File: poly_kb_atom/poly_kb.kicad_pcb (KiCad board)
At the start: 2 copper layers, 19.1 x 19 mm, 18 parts, among them J1 Conn_01x16, J2 North, J3 WestFront, J4 EastFront, J5 WestBack, J6 EastBack, J7 South, J8 North2, J9 South2, SW1 SW_Push

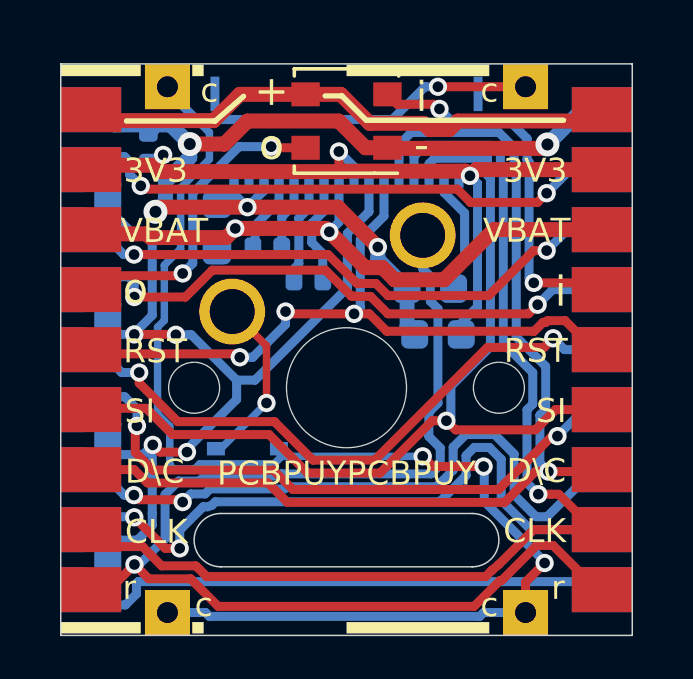
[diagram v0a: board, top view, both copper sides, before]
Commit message: Fixed wrong connection in between pin 16 an VCC in PolyAtom2; Added ConectorL
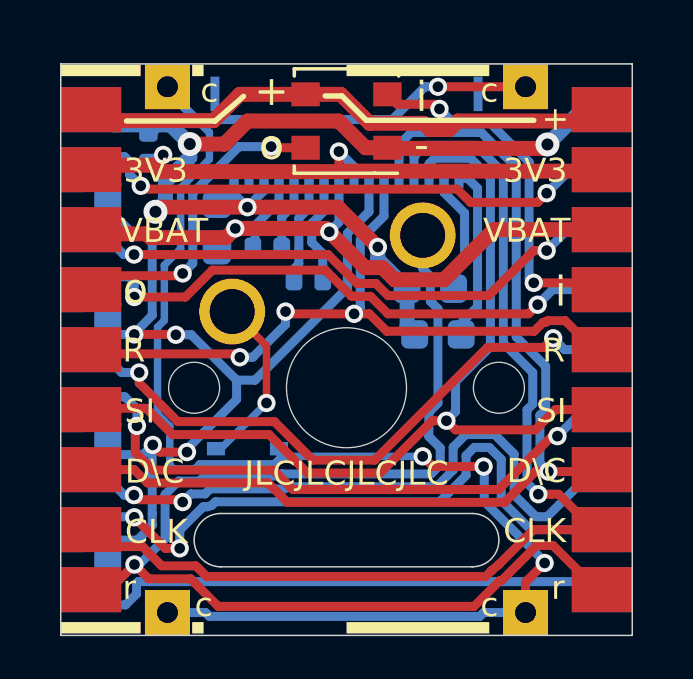
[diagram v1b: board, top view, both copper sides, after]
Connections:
- C1 pad 1: /Keyboard/sheet605ED2EB/3V3 -> Net-(C1-Pad1)
- J1 pad 16: /Keyboard/sheet605ED2EB/3V3 -> Net-(C1-Pad1)
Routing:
- net /Keyboard/sheet605ED2EB/3V3: track 25.8 -> 19.9 mm, vias 3 -> 2
- net Net-(C1-Pad1): track 0.00 -> 5.83 mm
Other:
- board text added: "+"
- board text added: ".1"
- board text added: "JLCJLCJLCJLC"
- board text added: "R"
- board text removed: "PCBPUYPCBPUY"
- board text removed: "RST"

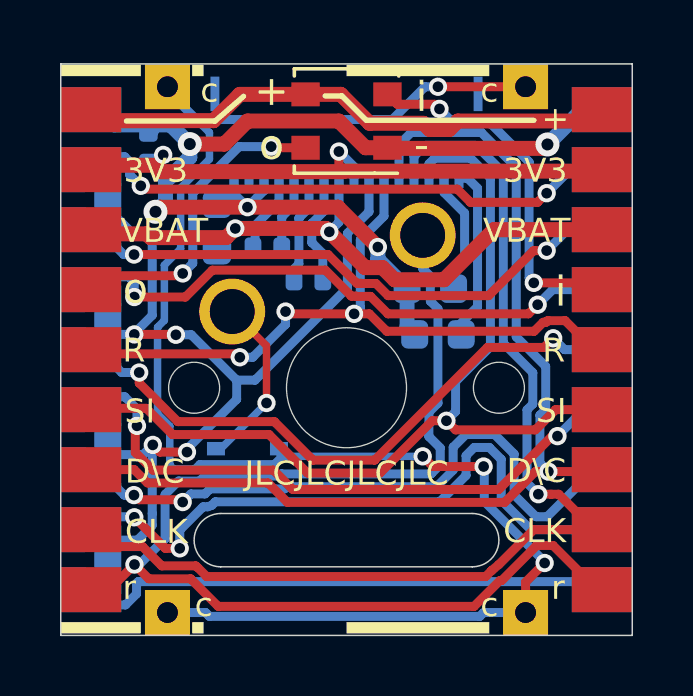
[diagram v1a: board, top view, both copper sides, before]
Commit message: Update to Kicad6 for PolyAtom and added a pullup resistor for CS
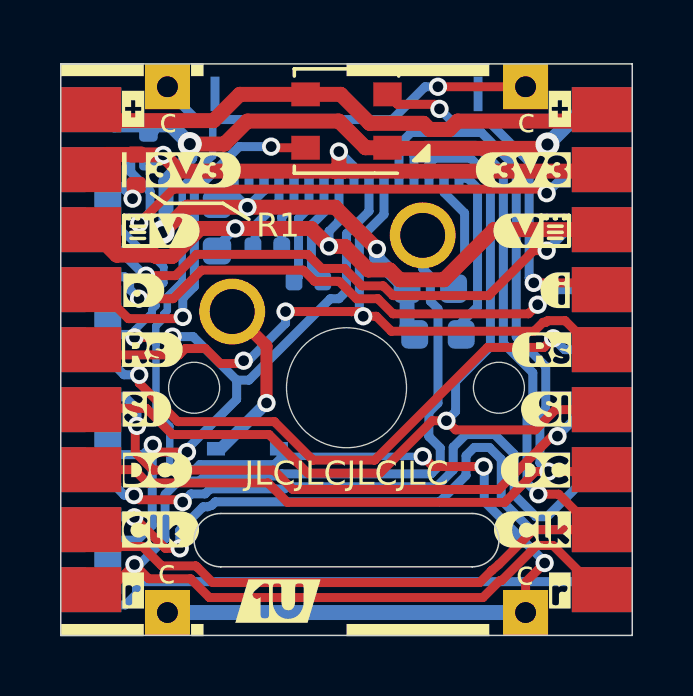
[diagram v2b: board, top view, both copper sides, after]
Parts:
- added R1: 1M, Resistor_SMD:R_0402_1005Metric, F.Cu at (263.5, 110.8)
- added kibuzzard-61EFA8F1: G***, kibuzzard-61EFA8F1, F.Cu at (276.7, 122.8)
- added kibuzzard-61EFAA6D: G***, kibuzzard-61EFAA6D, F.Cu at (277.0, 116.8)
- added kibuzzard-61EFABBF: G***, kibuzzard-61EFABBF, F.Cu at (276.8, 120.9)
- added kibuzzard-61EFACF9: G***, kibuzzard-61EFACF9, F.Cu at (276.2, 112.9)
- added kibuzzard-61EFBE21: G***, kibuzzard-61EFBE21, F.Cu at (263.9, 118.8)
- added kibuzzard-61EFBE2C: G***, kibuzzard-61EFBE2C, F.Cu at (264.2, 120.9)
- added kibuzzard-61EFBE3D: G***, kibuzzard-61EFBE3D, F.Cu at (264.3, 122.8)
- added kibuzzard-61EFBE87: G***, kibuzzard-61EFBE87, F.Cu at (264.8, 112.9)
- added kibuzzard-61EFD7F9: G***, kibuzzard-61EFD7F9, F.Cu at (277.2, 118.8)
- added kibuzzard-61EFD863: G***, kibuzzard-61EFD863, F.Cu at (276.4, 110.8)
- added kibuzzard-61EFD879: G***, kibuzzard-61EFD879, F.Cu at (265.4, 110.8)
- added kibuzzard-61EFD908: G***, kibuzzard-61EFD908, F.Cu at (263.4, 124.9)
- added kibuzzard-61EFD908: G***, kibuzzard-61EFD908, F.Cu at (277.6, 124.9)
- added kibuzzard-61EFD947: G***, kibuzzard-61EFD947, F.Cu at (277.6, 108.8)
- added kibuzzard-61EFD947: G***, kibuzzard-61EFD947, F.Cu at (263.4, 108.8)
- added kibuzzard-61EFDAA0: G***, kibuzzard-61EFDAA0, F.Cu at (263.8, 114.9)
- added kibuzzard-61EFDAC6: G***, kibuzzard-61EFDAC6, F.Cu at (277.6, 114.9)
- added kibuzzard-61EFDAEE: G***, kibuzzard-61EFDAEE, F.Cu at (264.0, 116.8)
- added kibuzzard-61EFDD1E: G***, kibuzzard-61EFDD1E, F.Cu at (268.2, 125.2)
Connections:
- J1 pad 2: (no net) -> unconnected-(J1-Pad2)
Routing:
- net /Keyboard/sheet605ED2EB/LED_DOUT: track 10.3 -> 12.8 mm
- net /Keyboard/sheet605ED2EB/CS: track 28.6 -> 30.5 mm, vias 4 -> 5
- net CS1: track 18.0 -> 19.8 mm
- net /Keyboard/sheet605ED2EB/4V2: track 21.1 -> 22.7 mm
- net /Keyboard/sheet605ED2EB/3V3: track 19.9 -> 21.1 mm
- net Net-(D1-Pad2): track 6.52 -> 5.89 mm
- net /Keyboard/sheet605ED2EB/KeyRow: track 40.1 -> 39.5 mm
- net CS2: track 18.3 -> 18.9 mm
- net /Keyboard/sheet605ED2EB/GND: track 35.8 -> 36.4 mm
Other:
- net class Default removed
- board text added: "C3"
- board text removed: "+"
- board text removed: "GND"
- board text removed: "pick one"
- board text removed: "r"

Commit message: Added new revisions for all pcbs expect 1.25U; cleaned up gerber dirs
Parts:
- D1: footprint Diode_SMD:D_SOD-323 -> poly_kb:D_SOD-323Ext
- R1: moved to B.Cu
- moved kibuzzard-61EFD879 177.7 mm to (95.8, 57.7)
- moved C4 177.1 mm to (104.3, 61.8)
- moved kibuzzard-61EFDD1E 177.0 mm to (99.4, 71.9)
- moved D1 177.0 mm to (98.4, 67.0)
- moved C3 177.0 mm to (95.1, 56.9)
- moved C6 177.0 mm to (100.5, 61.4)
- moved J4 177.0 mm to (110.2, 63.7)
- moved J6 177.0 mm to (110.2, 63.7)
- moved J7 177.0 mm to (95.8, 72.4)
- moved J8 177.0 mm to (95.8, 54.9)
- moved SW1 177.0 mm to (104.3, 59.9)
- moved kibuzzard-61EFA8F1 177.0 mm to (107.9, 69.7)
- moved kibuzzard-61EFAA6D 177.0 mm to (108.2, 63.7)
- moved kibuzzard-61EFBE21 177.0 mm to (95.1, 65.7)
- moved kibuzzard-61EFBE2C 177.0 mm to (95.4, 67.7)
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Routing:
- net /Keyboard/sheet605ED2EB/3V3: track 21.1 -> 25.2 mm, vias 2 -> 3
- net /Keyboard/sheet605ED2EB/GND: track 36.4 -> 38.2 mm, vias 5 -> 11
- net /Keyboard/sheet605ED2EB/5V: track 17.8 -> 19.5 mm
- net CS1: track 19.8 -> 18.1 mm
- net /Keyboard/sheet605ED2EB/SDIN: track 30.1 -> 31.8 mm
- net /Keyboard/sheet605ED2EB/4V2: track 22.7 -> 21.5 mm
- net CS2: track 18.9 -> 17.7 mm
- net /Keyboard/sheet605ED2EB/LED_DOUT: track 12.8 -> 11.8 mm
- net Net-(C5-Pad2): track 2.46 -> 1.78 mm
- net CS8: track 17.4 -> 17.9 mm
- net CS4: track 20.0 -> 20.6 mm
- net /Keyboard/sheet605ED2EB/SCLK: track 36.2 -> 36.7 mm
- net /Keyboard/sheet605ED2EB/CS: track 30.5 -> 30.0 mm, vias 5 -> 4
- added copper zone on B.Cu, net /Keyboard/sheet605ED2EB/GND
- added copper zone on F.Cu, net /Keyboard/sheet605ED2EB/GND
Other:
- board size 19.1 x 19 mm -> 19 x 19 mm
- board text added: "16"
- board text added: "D"
- board text added: "E"
- board text added: "L"
- board text removed: "3V3"
- board text removed: "CLK"
- board text removed: "D\C"
- board text removed: "R"
- board text removed: "SI"
- board text removed: "VBAT"
- board text removed: "i"
- board text removed: "o"

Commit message: Added optional C7 and fix LED silkscreens
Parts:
- added C7: 100nF, Capacitor_SMD:C_0603_1608Metric, F.Cu at (97.7, 56.1)
